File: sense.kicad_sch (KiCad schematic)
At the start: 35 parts, among them J6 Rudder, J7 End Stops, J8 Conn_01x02, J9 ISP, U4 AMS1117-5.0, U6 LM317, U7 ATmega328P-AU, Y1 8mhz

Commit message: Switch footprints to stock KiCad versions, if the stock one is equivalent
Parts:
- J9: footprint pypilot_footprints:PinHeader_2x03_P2.54mm_Vertical_SMD -> Connector_PinHeader_2.54mm:PinHeader_2x03_P2.54mm_Vertical_SMD
- U4: footprint pypilot_footprints:SOT-223-3_TabPin2_180 -> Package_TO_SOT_SMD:SOT-223-3_TabPin2
- U6: footprint pypilot_footprints:TO-252-2 -> Package_TO_SOT_SMD:TO-252-2
- U7: footprint pypilot_footprints:TQFP-32_7x7mm_P0.8mm -> Package_QFP:TQFP-32_7x7mm_P0.8mm
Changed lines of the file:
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@@
 			)
 		)
-		(property "Footprint" "pypilot_footprints:PinHeader_2x03_P2.54mm_Vertical_SMD"
+		(property "Footprint" "Connector_PinHeader_2.54mm:PinHeader_2x03_P2.54mm_Vertical_SMD"
 			(at 200.66 52.07 0)
 			(effects
@@
 			)
 		)
-		(property "Footprint" "pypilot_footprints:TO-252-2"
+		(property "Footprint" "Package_TO_SOT_SMD:TO-252-2"
 			(at 46.99 25.4 0)
 			(effects
@@
 			)
 		)
-		(property "Footprint" "pypilot_footprints:SOT-223-3_TabPin2_180"
+		(property "Footprint" "Package_TO_SOT_SMD:SOT-223-3_TabPin2"
 			(at 73.66 26.67 0)
 			(effects
@@
 			)
 		)
-		(property "Footprint" "pypilot_footprints:TQFP-32_7x7mm_P0.8mm"
+		(property "Footprint" "Package_QFP:TQFP-32_7x7mm_P0.8mm"
 			(at 120.65 81.28 0)
 			(effects

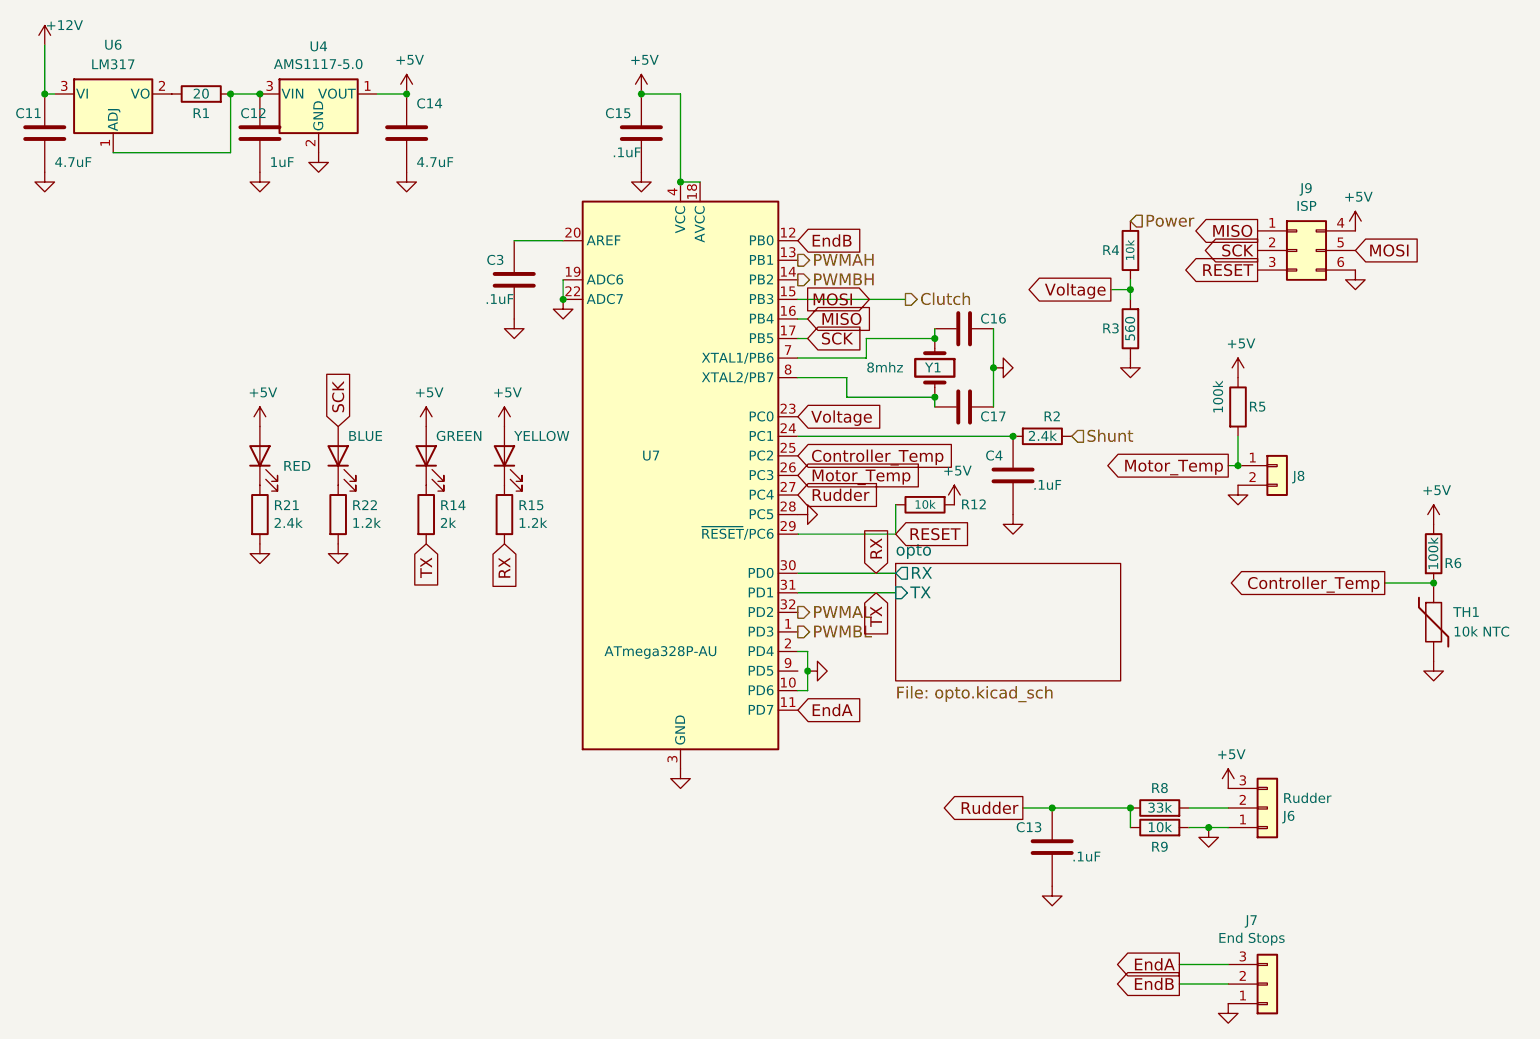
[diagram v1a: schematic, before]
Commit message: Use stock KiCad symbols instead of Freetronics ones.
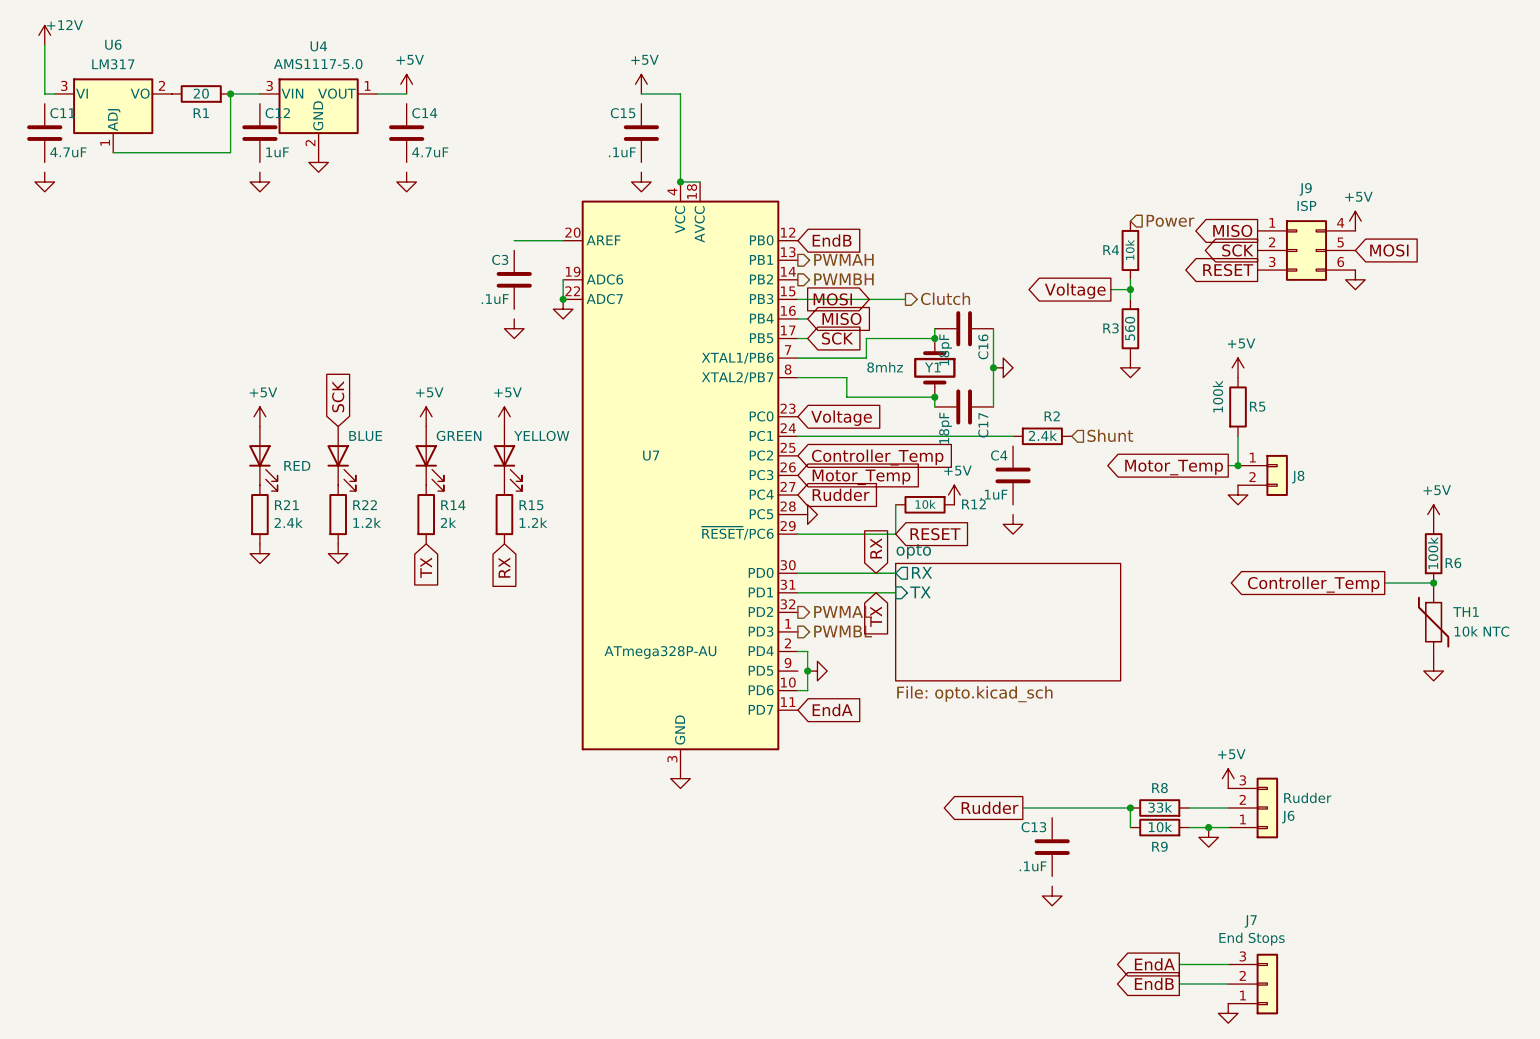
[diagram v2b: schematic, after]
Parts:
- C11, C12, C13, C14, C15, C3, C4: symbol freetronics_schematic:CAP -> Device:C
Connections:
- net +12V: no longer C11.1
- net +5V: no longer C14.1, C15.1
- net GND: no longer C11.2, C12.2, C13.2, C14.2, C15.2, C3.2, C4.2
- net Rudder: no longer C13.1
- net at R2.2, U7.24 (PC1): no longer C4.1
- net at R1.2, U4.3 (VIN), U6.1 (ADJ): no longer C12.1
- net at C3.1: no longer U7.20 (AREF)

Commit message: Reconnect caps
Stock symbols are smaller than the Freetronics ones were
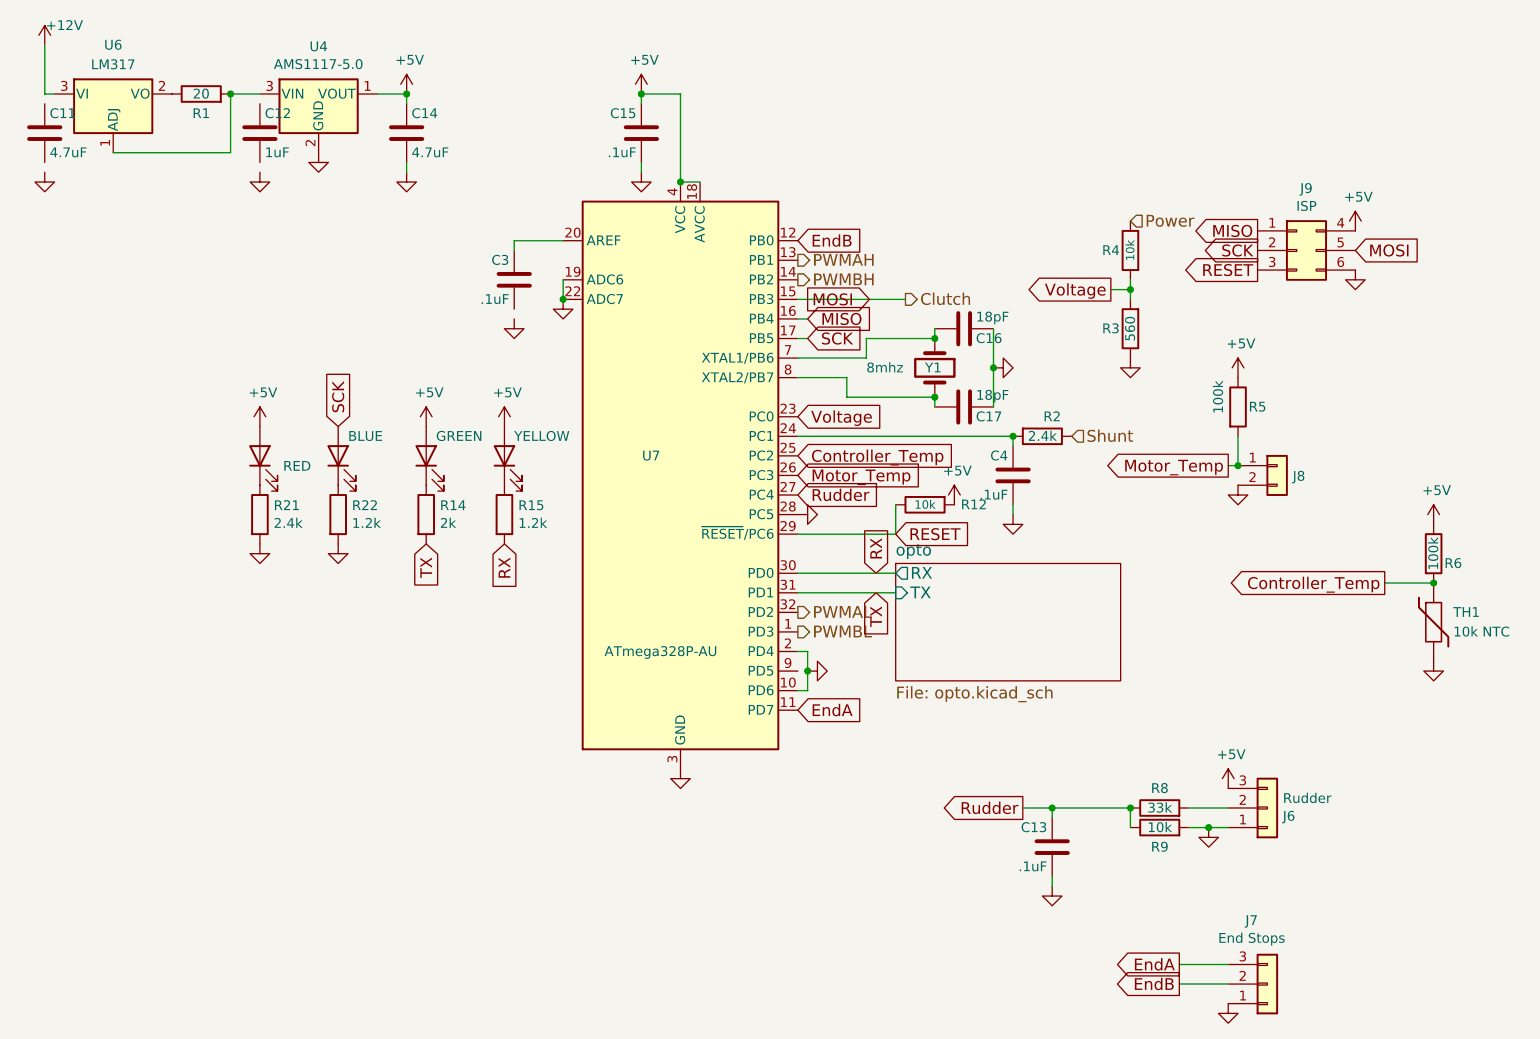
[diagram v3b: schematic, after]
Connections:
- net +5V: now also C14.1, C15.1
- net GND: now also C13.2, C14.2, C15.2, C4.2
- net Rudder: now also C13.1
- net at R2.2, U7.24 (PC1): now also C4.1
- net at C3.1: now also U7.20 (AREF)
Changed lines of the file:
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@@
 	)
 	(junction
+		(at 85.09 31.75)
+		(diameter 0)
+		(color 0 0 0 0)
+	)
+	(junction
+		(at 115.57 31.75)
+		(diameter 0)
+		(color 0 0 0 0)
+	)
+	(junction
 		(at 218.44 95.25)
 		(diameter 0)
@@
 	)
 	(junction
+		(at 163.83 76.2)
+		(diameter 0)
+		(color 0 0 0 0)
+	)
+	(junction
 		(at 179.07 124.46)
 		(diameter 0)
@@
 		(color 0 0 0 0)
 	)
+	(junction
+		(at 168.91 124.46)
+		(diameter 0)
+		(color 0 0 0 0)
+	)
 	(wire
 		(pts
@@
 	(wire
 		(pts
-			(xy 165.1 124.46) (xy 179.07 124.46)
+			(xy 165.1 124.46) (xy 168.91 124.46)
 		)
 		(stroke
@@
 	(wire
 		(pts
+			(xy 85.09 40.64) (xy 85.09 41.91)
+		)
+		(stroke
+			(width 0)
+			(type default)
+		)
+	)
+	(wire
+		(pts
+			(xy 115.57 31.75) (xy 115.57 33.02)
+		)
+		(stroke
+			(width 0)
+			(type default)
+		)
+	)
+	(wire
+		(pts
 			(xy 142.24 71.12) (xy 142.24 68.58)
 		)
@@
 	(wire
 		(pts
+			(xy 168.91 133.35) (xy 168.91 134.62)
+		)
+		(stroke
+			(width 0)
+			(type default)
+		)
+	)
+	(wire
+		(pts
 			(xy 153.67 71.12) (xy 153.67 72.39)
 		)
@@
 	(wire
 		(pts
+			(xy 99.06 50.8) (xy 99.06 52.07)
+		)
+		(stroke
+			(width 0)
+			(type default)
+		)
+	)
+	(wire
+		(pts
 			(xy 191.77 80.01) (xy 193.04 80.01)
 		)
@@
 	(wire
 		(pts
+			(xy 168.91 124.46) (xy 179.07 124.46)
+		)
+		(stroke
+			(width 0)
+			(type default)
+		)
+	)
+	(wire
+		(pts
 			(xy 46.99 39.37) (xy 62.23 39.37)
 		)
@@
 	(wire
 		(pts
+			(xy 168.91 124.46) (xy 168.91 125.73)
+		)
+		(stroke
+			(width 0)
+			(type default)
+		)
+	)
+	(wire
+		(pts
 			(xy 153.67 63.5) (xy 153.67 62.23)
 		)
@@
 	(wire
 		(pts
+			(xy 115.57 40.64) (xy 115.57 41.91)
+		)
+		(stroke
+			(width 0)
+			(type default)
+		)
+	)
+	(wire
+		(pts
 			(xy 144.78 63.5) (xy 153.67 63.5)
 		)
@@
 	(wire
 		(pts
+			(xy 163.83 85.09) (xy 163.83 86.36)
+		)
+		(stroke
+			(width 0)
+			(type default)
+		)
+	)
+	(wire
+		(pts
 			(xy 137.16 106.68) (xy 137.16 109.22)
 		)
@@
 	(wire
 		(pts
+			(xy 85.09 31.75) (xy 85.09 33.02)
+		)
+		(stroke
+			(width 0)
+			(type default)
+		)
+	)
+	(wire
+		(pts
 			(xy 189.23 127) (xy 186.69 127)
 		)
@@
 	(wire
 		(pts
+			(xy 163.83 76.2) (xy 163.83 77.47)
+		)
+		(stroke
+			(width 0)
+			(type default)
+		)
+	)
+	(wire
+		(pts
 			(xy 179.07 55.88) (xy 179.07 57.15)
 		)
@@
 		(dnp no)
 		(property "Reference" "C17"
-			(at 160.02 73.025 0)
+			(at 159.004 73.66 90)
 			(effects
 				(font
@@
 		)
 		(property "Value" "18pF"
-			(at 154.94 73.025 0)
+			(at 159.004 70.866 90)
 			(effects
 				(font
@@
 		(dnp no)
 		(property "Reference" "C16"
-			(at 160.02 62.865 0)
+			(at 159.004 63.5 90)
 			(effects
 				(font
@@
 		)
 		(property "Value" "18pF"
-			(at 154.94 62.865 0)
+			(at 159.004 60.706 90)
 			(effects
 				(font

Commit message: Replace 74AHC1G125 with 74LVC1G17
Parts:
- J9: symbol Connector_Generic:Conn_02x03_Top_Bottom -> Connector_Generic:Conn_02x03_Odd_Even
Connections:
- net +5V: no longer J9.4 (Pin_4)
- net GND: no longer J9.6 (Pin_6)
- net MISO: no longer J9.1 (Pin_1)
- net MOSI: no longer J9.5 (Pin_5)
- net RESET: no longer J9.3 (Pin_3)
- net SCK: no longer J9.2 (Pin_2)
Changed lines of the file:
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@@
 	)
 	(symbol
-		(lib_id "Connector_Generic:Conn_02x03_Top_Bottom")
+		(lib_id "Connector_Generic:Conn_02x03_Odd_Even")
 		(at 200.66 52.07 0)
 		(unit 1)
@@
 			)
 		)
-		(property "Datasheet" ""
+		(property "Datasheet" "~"
 			(at 200.66 52.07 0)
 			(effects
@@
 			)
 		)
-		(property "Description" ""
+		(property "Description" "Generic connector, double row, 02x03, odd/even pin numbering scheme (row 1 odd numbers, row 2 even numbers), script generated (kicad-library-utils/schlib/autogen/connector/)"
 			(at 200.66 52.07 0)
 			(effects

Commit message: Fix symbol for ISP header
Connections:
- net +5V: now also J9.4 (Pin_4)
- net GND: now also J9.6 (Pin_6)
- net MISO: now also J9.1 (Pin_1)
- net MOSI: now also J9.5 (Pin_5)
- net RESET: now also J9.3 (Pin_3)
- net SCK: now also J9.2 (Pin_2)

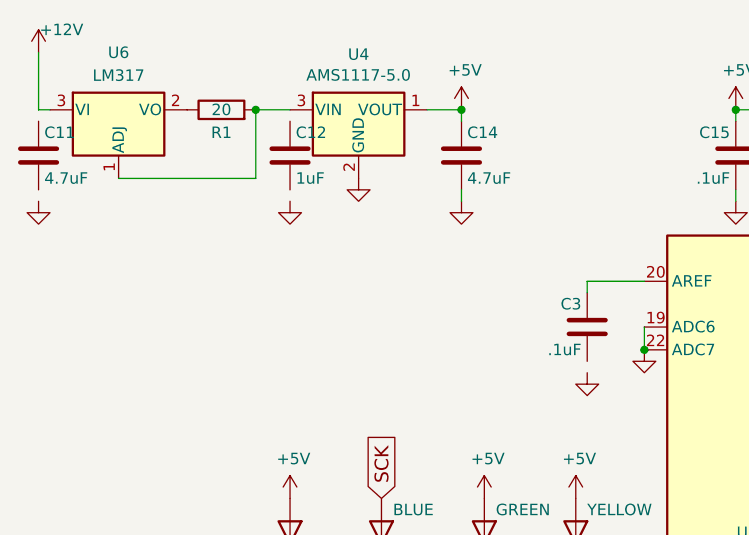
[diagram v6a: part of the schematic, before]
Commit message: Fix missing wires around smaller cap symbols
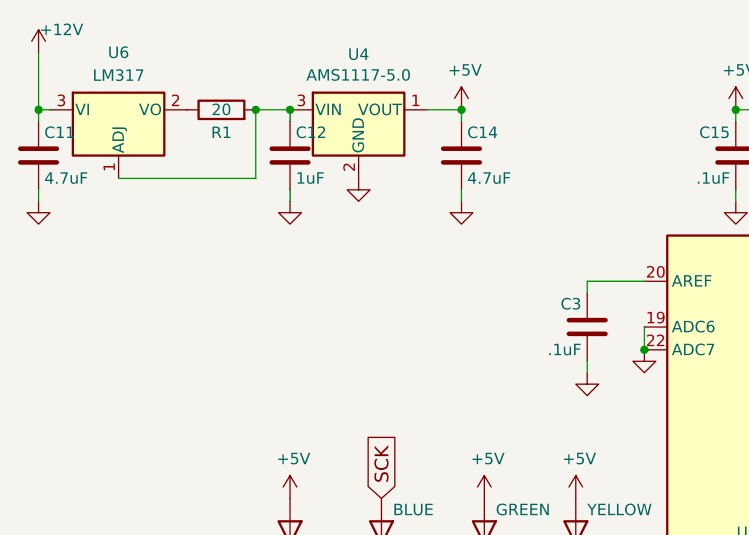
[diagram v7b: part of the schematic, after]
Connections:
- net +12V: now also C11.1
- net GND: now also C11.2, C12.2, C3.2
- net at R1.2, U4.3 (VIN), U6.1 (ADJ): now also C12.1
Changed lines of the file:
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@@
+	)
+	(junction
+		(at 66.04 31.75)
+		(diameter 0)
+		(color 0 0 0 0)
 	)
 	(junction
@@
 	)
 	(junction
+		(at 38.1 31.75)
+		(diameter 0)
+		(color 0 0 0 0)
+	)
+	(junction
 		(at 153.67 63.5)
 		(diameter 0)
@@
 	(wire
 		(pts
+			(xy 38.1 31.75) (xy 38.1 33.02)
+		)
+		(stroke
+			(width 0)
+			(type default)
+		)
+	)
+	(wire
+		(pts
 			(xy 142.24 71.12) (xy 142.24 68.58)
 		)
@@
 	(wire
 		(pts
+			(xy 38.1 40.64) (xy 38.1 41.91)
+		)
+		(stroke
+			(width 0)
+			(type default)
+		)
+	)
+	(wire
+		(pts
 			(xy 168.91 133.35) (xy 168.91 134.62)
 		)
@@
 	(wire
 		(pts
+			(xy 99.06 59.69) (xy 99.06 60.96)
+		)
+		(stroke
+			(width 0)
+			(type default)
+		)
+	)
+	(wire
+		(pts
 			(xy 135.89 88.9) (xy 148.59 88.9)
 		)
@@
 	(wire
 		(pts
+			(xy 66.04 31.75) (xy 66.04 33.02)
+		)
+		(stroke
+			(width 0)
+			(type default)
+		)
+	)
+	(wire
+		(pts
 			(xy 135.89 76.2) (xy 163.83 76.2)
 		)
@@
 		)
 		(stroke
+			(width 0)
+			(type default)
+		)
+	)
+	(wire
+		(pts
+			(xy 66.04 40.64) (xy 66.04 41.91)
+		)
+		(stroke

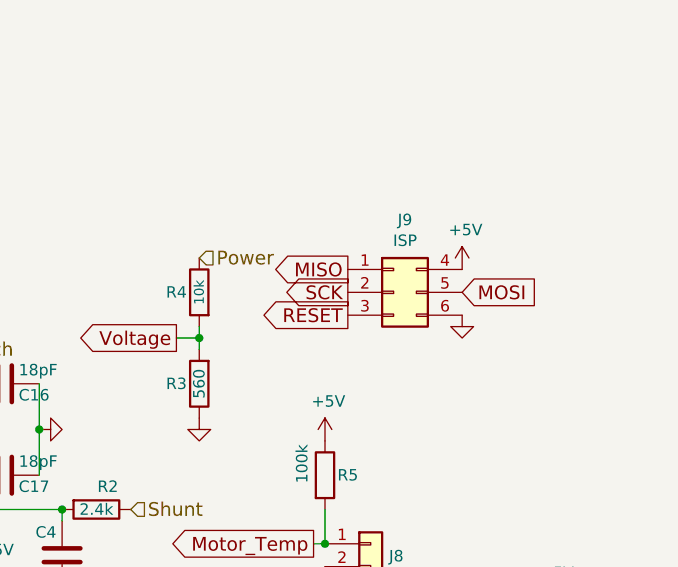
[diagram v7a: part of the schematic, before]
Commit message: Updated symbol for ISP header
Numbering was still set to old order
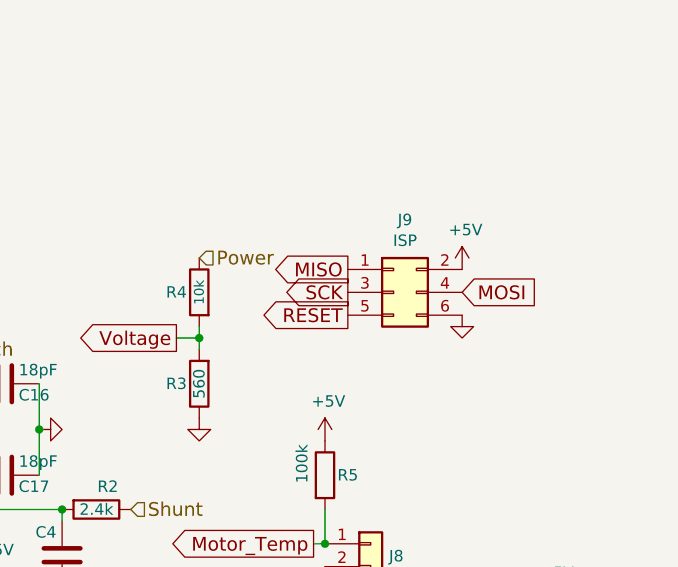
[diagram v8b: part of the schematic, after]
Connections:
- net +5V: now also J9.2 (Pin_2); no longer J9.4 (Pin_4)
- net MOSI: now also J9.4 (Pin_4); no longer J9.5 (Pin_5)
- net RESET: now also J9.5 (Pin_5); no longer J9.3 (Pin_3)
- net SCK: now also J9.3 (Pin_3); no longer J9.2 (Pin_2)
